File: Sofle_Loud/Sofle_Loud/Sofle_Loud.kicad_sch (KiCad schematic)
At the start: 76 parts, among them J1 Pimaroni Trackball, J2 4PIN, J3 OLED, Q2 TIP120, SW1 SW_PUSH_LED, SW10 SW_PUSH_LED, SW11 SW_PUSH_LED, SW12 SW_PUSH_LED, SW13 SW_PUSH_LED, SW14 SW_PUSH_LED, SW15 SW_PUSH_LED, SW16 SW_PUSH_LED, SW17 SW_PUSH_LED, SW18 SW_PUSH_LED, SW19 SW_PUSH_LED, SW2 SW_PUSH_LED, SW20 SW_PUSH_LED, SW21 SW_PUSH_LED, SW22 SW_PUSH_LED, SW23 SW_PUSH_LED, SW24 SW_PUSH_LED, SW25 Rotary_Encoder_Switch, SW26 SW_PUSH_LED, SW27 SW_PUSH_LED, SW28 SW_PUSH_LED, SW29 SW_PUSH_LED, SW3 SW_PUSH_LED, SW30 SW_PUSH_LED, SW4 SW_PUSH_LED, SW5 SW_PUSH_LED, SW6 SW_PUSH_LED, SW7 SW_PUSH_LED, SW8 SW_PUSH_LED, SW9 SW_PUSH_LED, U1 ProMicro_Choc_MX

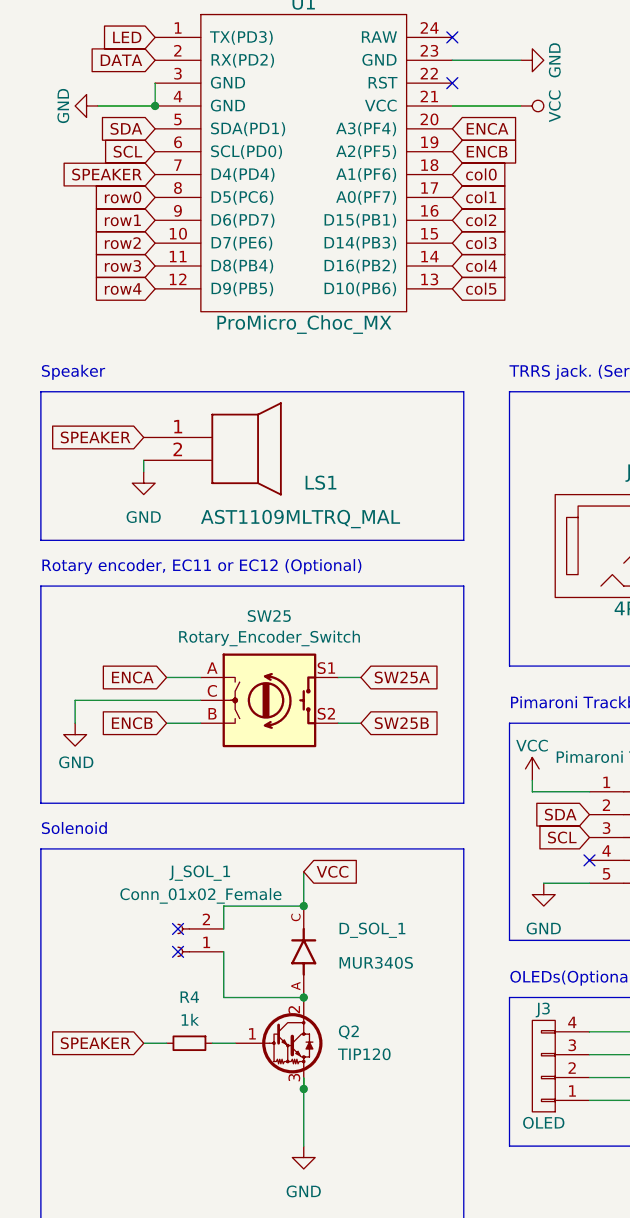
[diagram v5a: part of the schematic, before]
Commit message: Revised Main board outline Solenoid should now attach to bottom plate Removed speaker Rerouted for new plate cutouts
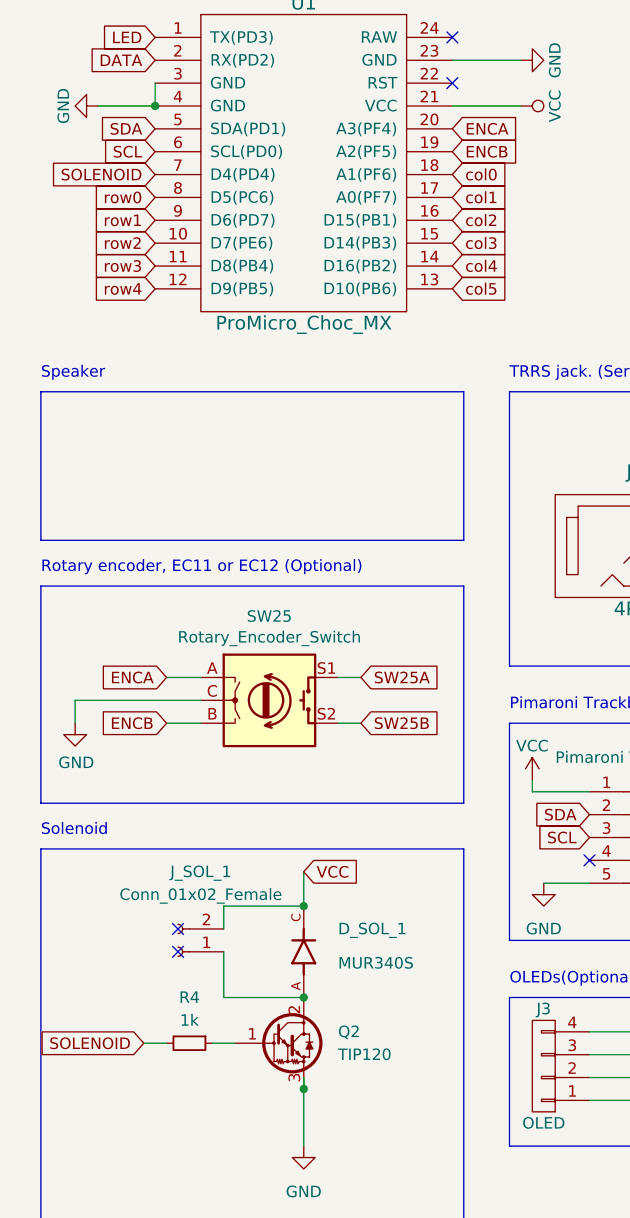
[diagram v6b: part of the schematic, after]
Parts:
- removed LS1: AST1109MLTRQ_MAL, SofleChocLoud:AST1109MLTRQ, symbol AST1109MLTRQ:AST1109MLTRQ
- Q2: footprint SofleChocLoud:TO-220-3_Horizontal_TabUp -> SofleChocLoud:TO-220-3_Horizontal_TabUp_noHeatsink
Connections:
- net SPEAKER renamed SOLENOID
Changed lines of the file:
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@@
     (stroke (width 0) (type default))
   )
-  (wire (pts (xy 26.67 69.85) (xy 26.67 68.58))
-    (stroke (width 0) (type default))
-  )
   (wire (pts (xy 261.62 120.65) (xy 261.62 104.14))
     (stroke (width 0) (type default))
@@
     )
   )
-  (global_label "LED" (shape input) (at 179.07 21.59 180)
+  (global_label "SOLENOID" (shape input) (at 27.94 36.83 180) (fields_autoplaced)
     (effects (font (size 1.27 1.27)) (justify right))
-    (property "Intersheetrefs" "${INTERSHEET_REFS}" (at 179.07 21.59 0)
-      (effects (font (size 1.27 1.27)) hide)
+    (property "Intersheetrefs" "${INTERSHEET_REFS}" (at 16.4355 36.83 0)
+      (effects (font (size 1.27 1.27)) (justify right) hide)
     )
   )
-  (global_label "SPEAKER" (shape input) (at 26.67 66.04 180) (fields_autoplaced)
+  (global_label "LED" (shape input) (at 179.07 21.59 180)
     (effects (font (size 1.27 1.27)) (justify right))
-    (property "Intersheetrefs" "${INTERSHEET_REFS}" (at 15.8507 65.9606 0)
-      (effects (font (size 1.27 1.27)) (justify right) hide)
+    (property "Intersheetrefs" "${INTERSHEET_REFS}" (at 179.07 21.59 0)
+      (effects (font (size 1.27 1.27)) hide)
     )
   )
@@
     )
   )
+  (global_label "SOLENOID" (shape input) (at 26.67 133.35 180) (fields_autoplaced)
+    (effects (font (size 1.27 1.27)) (justify right))
+    (property "Intersheetrefs" "${INTERSHEET_REFS}" (at 15.1655 133.35 0)
+      (effects (font (size 1.27 1.27)) (justify right) hide)
+    )
+  )
   (global_label "row4" (shape input) (at 27.94 49.53 180)
     (effects (font (size 1.27 1.27)) (justify right))
@@
     )
   )
-  (global_label "SPEAKER" (shape input) (at 27.94 36.83 180) (fields_autoplaced)
-    (effects (font (size 1.27 1.27)) (justify right))
-    (property "Intersheetrefs" "${INTERSHEET_REFS}" (at 17.1207 36.7506 0)
-      (effects (font (size 1.27 1.27)) (justify right) hide)
-    )
-  )
   (global_label "ENCA" (shape input) (at 60.96 31.75 0)
     (effects (font (size 1.27 1.27)) (justify left))
@@
     )
   )
-  (global_label "SPEAKER" (shape input) (at 26.67 133.35 180) (fields_autoplaced)
-    (effects (font (size 1.27 1.27)) (justify right))
-    (property "Intersheetrefs" "${INTERSHEET_REFS}" (at 16.0123 133.35 0)
-      (effects (font (size 1.27 1.27)) (justify right) hide)
-    )
-  )
   (global_label "col5" (shape input) (at 60.96 49.53 0)
     (effects (font (size 1.27 1.27)) (justify left))
@@
       (effects (font (size 1.27 1.27)) (justify left))
     )
-    (property "Footprint" "SofleChocLoud:TO-220-3_Horizontal_TabUp" (at 46.99 135.255 0)
+    (property "Footprint" "SofleChocLoud:TO-220-3_Horizontal_TabUp_noHeatsink" (at 46.99 135.255 0)
       (effects (font (size 1.27 1.27) italic) (justify left) hide)
     )
@@
     )
   )
-  (symbol (lib_id "power:GND") (at 26.67 69.85 0) (mirror y) (unit 1)
-    (in_bom yes) (on_board yes) (dnp no) (fields_autoplaced)
-    (property "Reference" "#PWR014" (at 26.67 76.2 0)
-      (effects (font (size 1.27 1.27)) hide)
-    )
-    (property "Value" "GND" (at 26.67 74.93 0)
-      (effects (font (size 1.27 1.27)))
-    )
-    (property "Footprint" "" (at 26.67 69.85 0)
-      (effects (font (size 1.27 1.27)) hide)
-    )
-    (property "Datasheet" "" (at 26.67 69.85 0)
-      (effects (font (size 1.27 1.27)) hide)
-    )
-    (pin "1")
-    (instances
-      (project "Sofle_Loud"
-        (path "/06057b3a-55ab-4f4e-913e-2aeec5ff3587"
-          (reference "#PWR014") (unit 1)
-        )
-      )
-      (project "ergodonk_pcb"
-        (path "/ed1aaf15-4e1f-4159-b371-d99b3fb972ad"
-          (reference "#PWR0101") (unit 1)
-        )
-      )
-    )
-  )
   (symbol (lib_id "SofleKeyboard-rescue:VCC-power") (at 81.28 134.62 270) (unit 1)
     (in_bom yes) (on_board yes) (dnp no)
@@
         )
       )
-    )
-  )
-  (symbol (lib_id "AST1109MLTRQ:AST1109MLTRQ") (at 26.67 66.04 0) (unit 1)
-    (in_bom yes) (on_board yes) (dnp no)
-    (property "Reference" "LS1" (at 44.45 71.12 0)
-      (effects (font (size 1.524 1.524)) (justify left))
-    )
-    (property "Value" "AST1109MLTRQ_MAL" (at 33.02 74.93 0)
-      (effects (font (size 1.524 1.524)) (justify left))
-    )
-    (property "Footprint" "SofleChocLoud:AST1109MLTRQ" (at 34.29 62.484 0)
-      (effects (font (size 1.524 1.524)) hide)
-    )
-    (property "Datasheet" "" (at 26.67 66.04 0)
-      (effects (font (size 1.524 1.524)))
-    )
-    (pin "1")
-    (pin "2")
-    (instances
-      (project "Sofle_Loud"
-        (path "/06057b3a-55ab-4f4e-913e-2aeec5ff3587"
-          (reference "LS1") (unit 1)
-        )
-      )
-      (project "ergodonk_pcb"
-        (path "/ed1aaf15-4e1f-4159-b371-d99b3fb972ad"
-          (reference "LS1") (unit 1)
-        )
-      )
